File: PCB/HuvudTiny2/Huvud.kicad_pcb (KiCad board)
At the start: 4 copper layers, 42 x 42 mm, 98 parts, among them J1 Vin, J10 TC2, J12 USB_Micro-B, J2 DBG, J3 THERM, J4 FAN0, J5 FAN1, J6 Heater, J7 Endstop, J8 TC1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

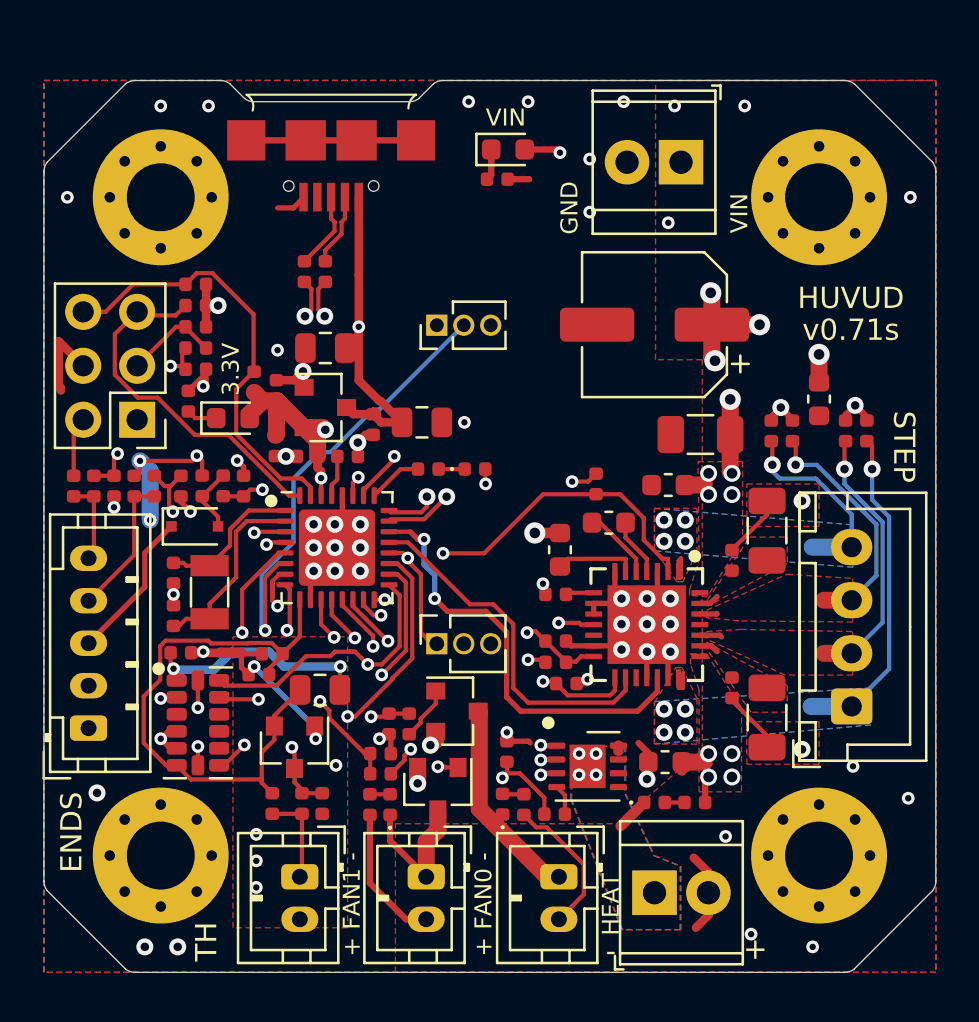
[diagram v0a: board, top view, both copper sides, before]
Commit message: Update PT board size and move filter cap on the Huvud so ethe two boards can actually be attached together.
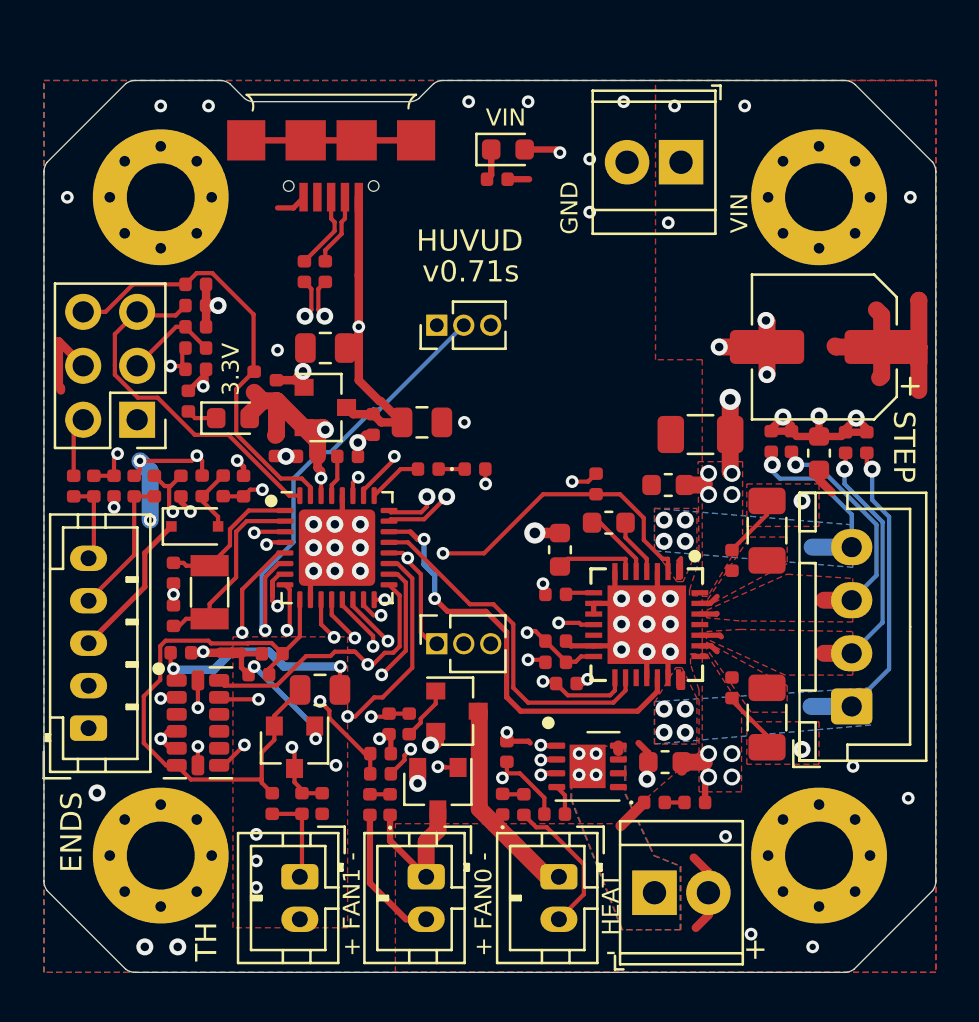
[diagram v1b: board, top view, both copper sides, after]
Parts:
- moved C8 8.07 mm to (218.8, 112.5)
- moved C16 2.55 mm to (218.5, 117.5), turned to 90 degrees
- moved C26 0.55 mm to (220.8, 117.0)
- moved C28 0.55 mm to (219.8, 117.0)
- moved C21 0.50 mm to (217.2, 117.0)
- moved C20 0.50 mm to (216.2, 117.0)
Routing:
- net GND: track 55.1 -> 65.6 mm, vias 57 -> 61
- net ST_VS: track 36.2 -> 43.0 mm, vias 24 -> 20
- net /ST_A2: track 17.0 -> 16.4 mm
- net /ST_A1: track 13.7 -> 13.2 mm
- net /ST_B2: track 11.0 -> 10.5 mm

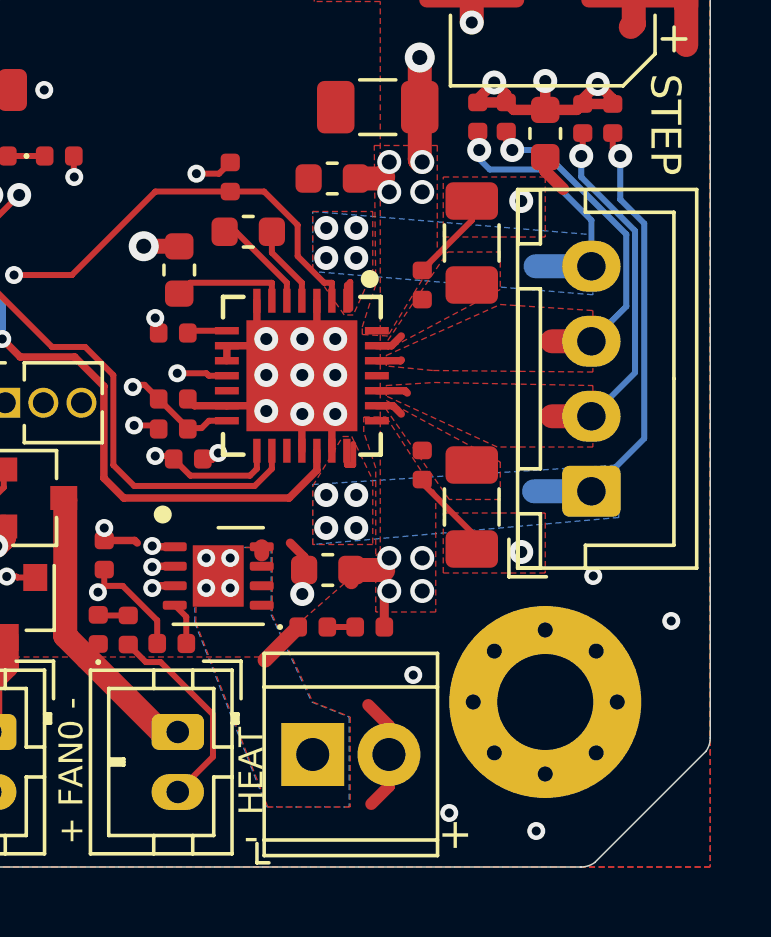
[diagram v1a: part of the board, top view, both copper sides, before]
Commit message: Improve sense resistor ground. Improve power mosfer routing. Set PCB color and copper finish.
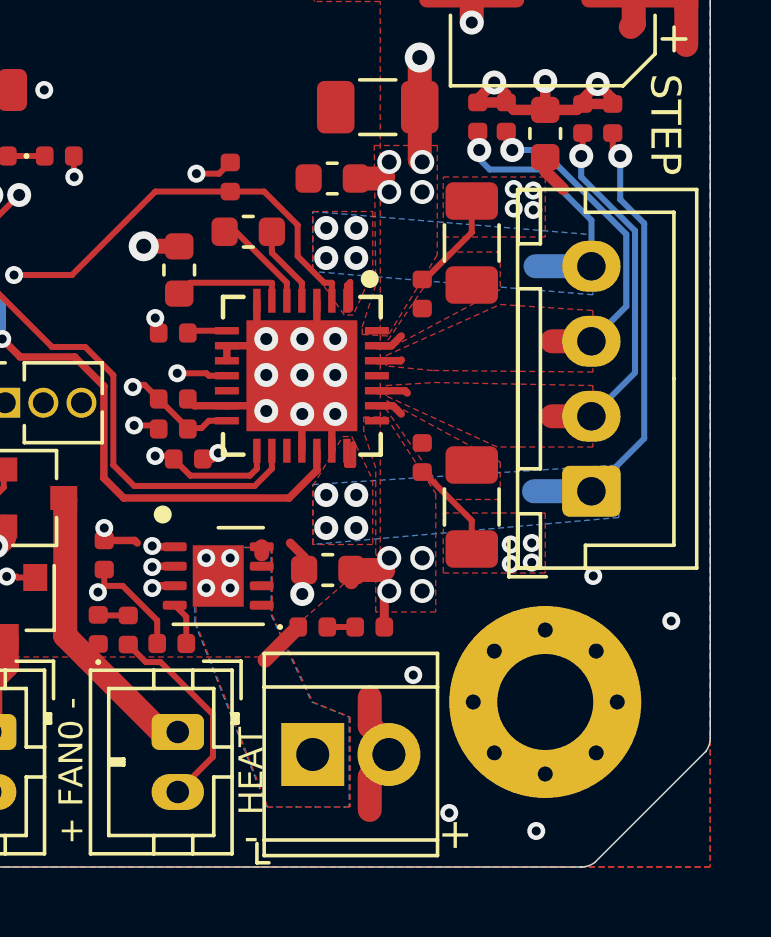
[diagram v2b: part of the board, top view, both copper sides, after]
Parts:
- moved C29 0.30 mm to (214.4, 122.9)
- moved C36 0.25 mm to (214.4, 128.3)
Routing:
- net ST_VS: track 43.0 -> 48.4 mm
- net GND: track 65.6 -> 66.2 mm, vias 61 -> 67
- added copper zone on In1.Cu, net Net-(D3-Pad1)

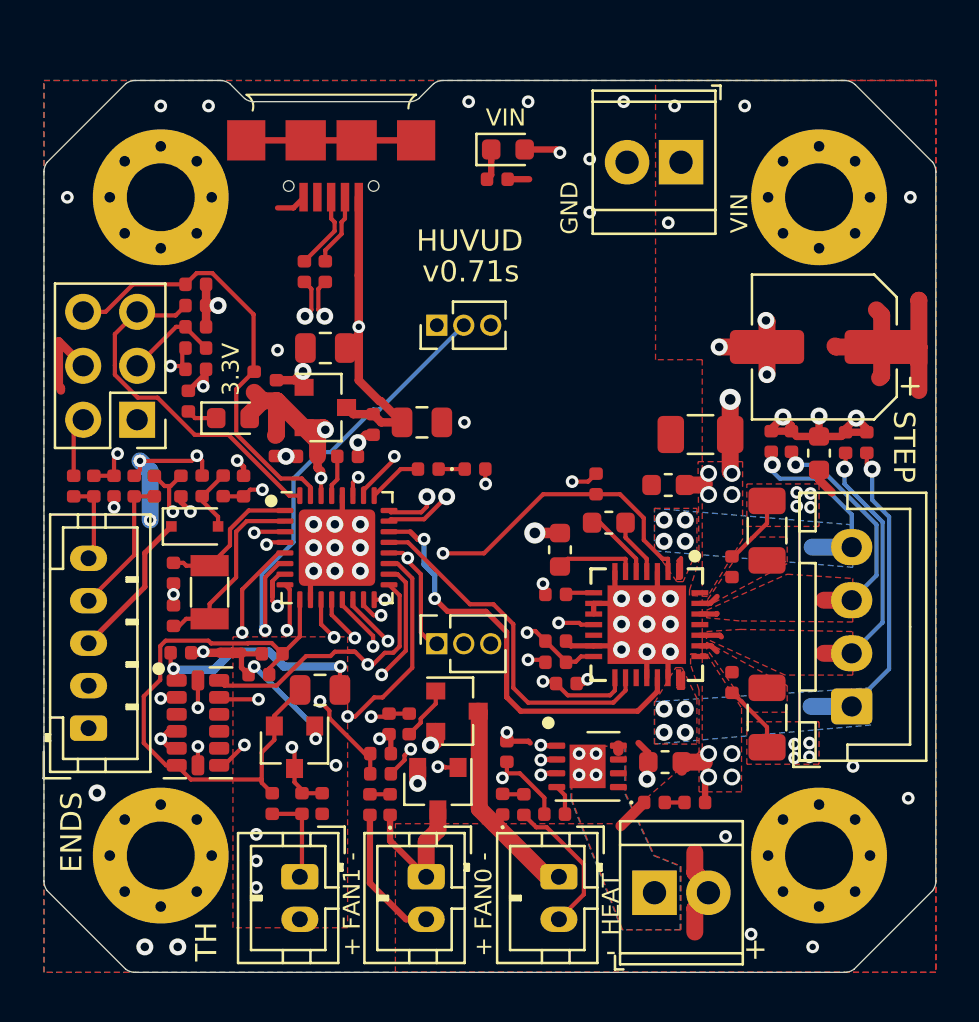
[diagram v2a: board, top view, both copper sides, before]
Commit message: Route new version with 1.25mm connectors. Added TH2 and 24V on the endstop connector.
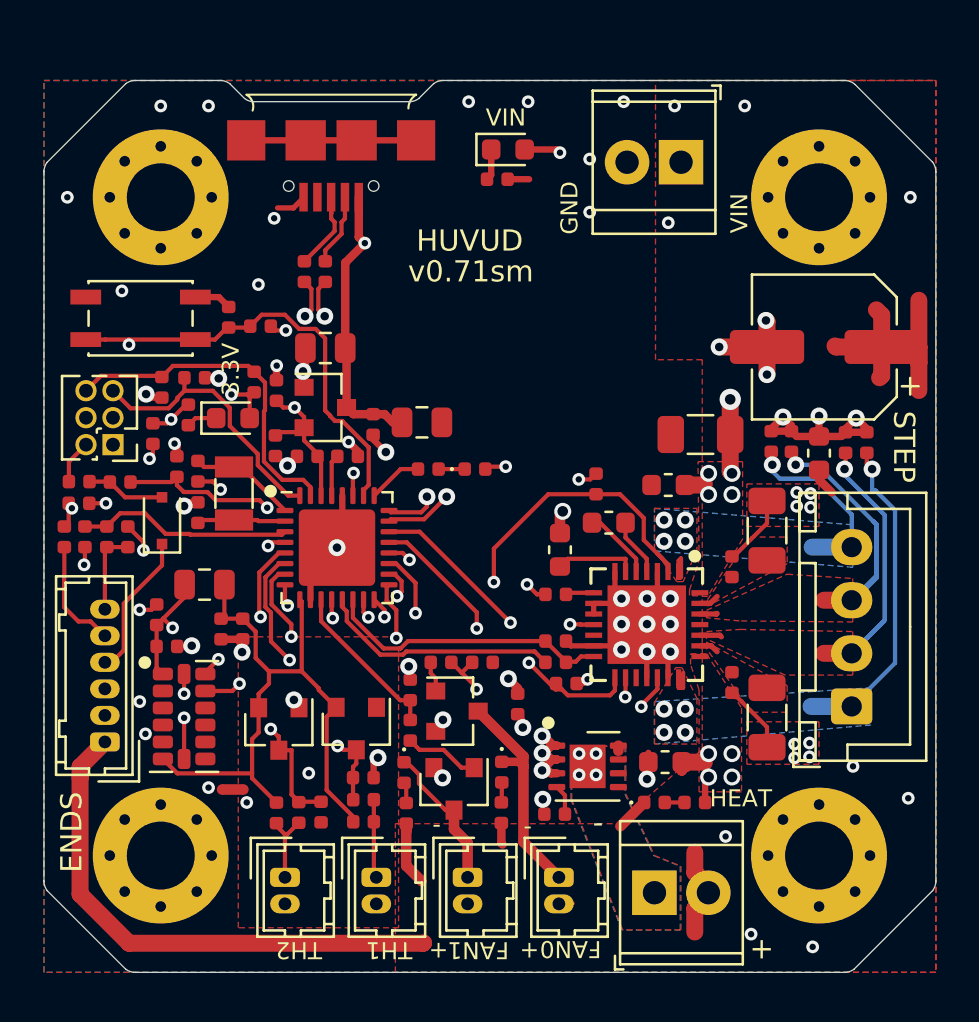
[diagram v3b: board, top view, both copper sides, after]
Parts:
- removed J10: TC2, Connector_PinHeader_1.27mm:PinHeader_1x03_P1.27mm_Vertical
- added C1: 0.1uF, Capacitor_SMD:C_0402_1005Metric, F.Cu at (195.1, 134.4)
- added D7: BAT54S, Package_TO_SOT_SMD:SOT-23, F.Cu at (193.1, 130.5)
- added R17: 10k, Resistor_SMD:R_0402_1005Metric, F.Cu at (194.0, 134.5)
- added R9: 4.7k, Resistor_SMD:R_0402_1005Metric, F.Cu at (192.9, 134.5)
- added SW1: SW_Push, Button_Switch_SMD:SW_SPST_EVQP2, F.Cu at (186.6, 111.2)
- J2: footprint Connector_PinHeader_2.54mm:PinHeader_2x03_P2.54mm_Vertical -> Connector_PinHeader_1.27mm:PinHeader_2x03_P1.27mm_Vertical
- J3, J4, J5: footprint Connector_JST:JST_PH_B2B-PH-K_1x02_P2.00mm_Vertical -> Connector_Hirose:Hirose_DF13-02P-1.25DSA_1x02_P1.25mm_Vertical
- J7: footprint Connector_JST:JST_PH_B5B-PH-K_1x05_P2.00mm_Vertical -> Connector_Hirose:Hirose_DF13-06P-1.25DSA_1x06_P1.25mm_Vertical
- J8: value TC1 -> THERM; footprint Connector_PinSocket_1.27mm:PinSocket_1x03_P1.27mm_Vertical -> Connector_Hirose:Hirose_DF13-02P-1.25DSA_1x02_P1.25mm_Vertical
- moved J8 13.1 mm to (193.3, 137.5), turned to -90 degrees
- moved L1 7.36 mm to (189.6, 123.7), turned to 0 degrees
- moved NT1 6.44 mm to (190.9, 133.4)
- moved R42 6.15 mm to (187.3, 125.2), turned to -90 degrees
- moved R32 5.79 mm to (183.7, 118.9), turned to 0 degrees
- moved R8 5.27 mm to (202.7, 127.4), turned to 180 degrees
- moved R21 5.11 mm to (187.6, 114.5), turned to 90 degrees
- moved C12 4.98 mm to (189.2, 120.3)
- moved C13 4.94 mm to (189.2, 118.4)
- moved C31 4.87 mm to (183.7, 119.9), turned to 0 degrees
- moved R43 4.87 mm to (183.0, 121.5)
- moved R33 4.85 mm to (185.6, 118.9), turned to 0 degrees
- moved Y1 4.79 mm to (190.9, 119.5)
- moved R2 4.39 mm to (197.1, 134.9), turned to 180 degrees
- moved C24 3.64 mm to (187.1, 116.6), turned to 90 degrees
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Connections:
- net THERM renamed THERM1
- J7 pad 1: GND -> ST_VS
- J7 pad 2: +5V -> GND
- J7 pad 3: Net-(D4-Pad1) -> +5V
- J7 pad 4: Net-(J7-Pad4) -> Net-(D4-Pad1)
- J8 pad 1: SDO -> Net-(J8-Pad1)
- J8 pad 2: SCL -> GNDA
- R19 pad 1: Net-(J7-Pad5) -> Net-(J7-Pad6)
- R36 pad 1: Net-(J7-Pad5) -> Net-(J7-Pad6)
- R42 pad 1: Net-(J7-Pad4) -> Net-(J7-Pad5)
- R43 pad 1: Net-(J7-Pad4) -> Net-(J7-Pad5)
- U1 pad 8: AINT1 -> (no net)
- U3 pad 5: AINT1 -> THERM2
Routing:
- net THERM1: track 31.9 -> 13.9 mm
- net +3V3: track 44.0 -> 29.1 mm, vias 10 -> 8
- net ST_VS: track 48.4 -> 63.1 mm
- net THERM2: track 0.00 -> 14.6 mm, vias 0 -> 2
- net AINT1: track 11.7 -> 0.00 mm, vias 2 -> 0
- net Net-(J7-Pad4): track 6.76 -> 0.00 mm
- net SCL: track 21.0 -> 14.4 mm
- net SDI: track 20.1 -> 14.6 mm, vias 1 -> 2
- net Net-(C12-Pad2): track 8.96 -> 4.18 mm
- net GNDA: track 7.87 -> 3.13 mm, vias 6 -> 5
- net ENDSTOP2: track 15.1 -> 19.8 mm
- net SWCLK: track 20.5 -> 16.1 mm
- net Net-(J7-Pad5): track 3.97 -> 8.36 mm, vias 0 -> 1
- net /ST_B1: track 11.8 -> 16.2 mm
- net FAN0: track 9.85 -> 14.0 mm
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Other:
- board text added: "FAN0"
- board text added: "FAN1"
- board text added: "IO RST nc"
- board text added: "TH1"
- board text added: "TH2"
- board text added: "Vin"
- board text added: "v0.71sm"
- board text removed: "+ FAN0 -"
- board text removed: "+ FAN1 -"
- board text removed: "3.3"
- board text removed: "CS"
- board text removed: "IO RST B1"
- board text removed: "SCL"
- board text removed: "SDI"
- board text removed: "SDO"
- board text removed: "TH"
- board text removed: "v0.71s"

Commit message: Switched power & USB to MOLEX MicroFit 2x6. Switched heater to 3.5mm terminal.
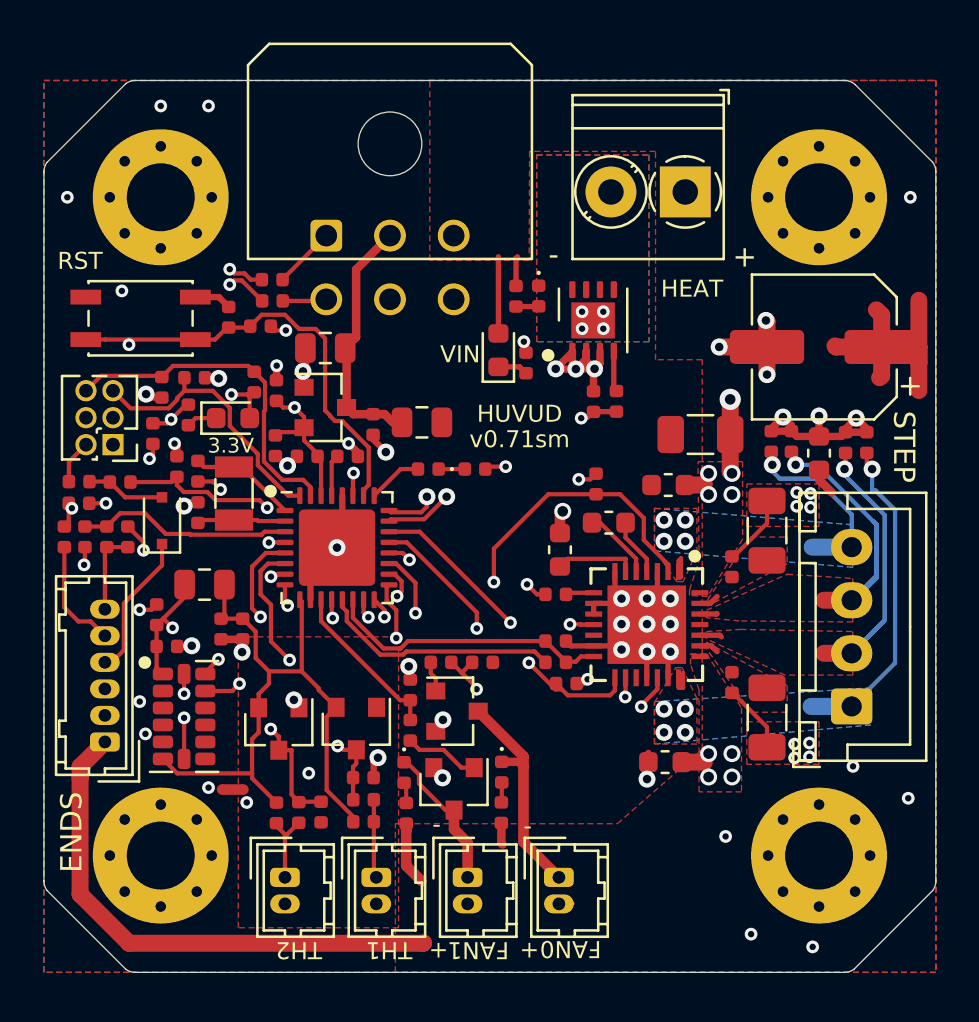
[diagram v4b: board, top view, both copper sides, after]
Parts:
- removed J12: USB_Micro-B, Huvud:MC-101C
- J1: value Vin -> MOLEX Micro Fit 2x3; footprint Huvud:TerminalBlock_TE_282834-2_1x02_P2.54mm_Horizontal -> Connector_Molex:Molex_Micro-Fit_3.0_43045-0600_2x03_P3.00mm_Horizontal
- J6: footprint Huvud:TerminalBlock_TE_282834-2_1x02_P2.54mm_Horizontal -> Huvud:TerminalBlock_Phoenix_PT-1,5-2-3.5-H_1x02_P3.50mm_Horizontal
- moved J6 33.0 mm to (212.2, 105.2), turned to 180 degrees
- moved R15 25.3 mm to (204.2, 110.2), turned to -90 degrees
- moved D3 24.5 mm to (205.3, 110.2), turned to -90 degrees
- moved Q3 21.0 mm to (207.9, 111.3), turned to 90 degrees
- moved R28 19.7 mm to (209.0, 115.1), turned to 90 degrees
- moved LOGO1 17.2 mm to (205.7, 132.2)
- moved J1 17.1 mm to (195.3, 107.3), turned to 0 degrees
- moved R12 14.7 mm to (207.9, 115.1)
- moved D6 9.46 mm to (203.4, 112.7), turned to 90 degrees
- moved R11 8.75 mm to (204.7, 113.3), turned to 90 degrees
- moved R26 2.53 mm to (192.8, 109.4), turned to 0 degrees
- moved R25 2.04 mm to (192.8, 110.4), turned to 0 degrees
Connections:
- J1 pad 1: ST_VS -> /D-
- J1 pad 2: GND -> +5V
- J6 pad 1: Net-(D3-Pad1) -> ST_VS
- J6 pad 2: ST_VS -> Net-(D3-Pad1)
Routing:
- net unconnected-(J12-Pad6): track 8.00 -> 0.00 mm
- net HEATER: track 22.7 -> 30.4 mm, vias 3 -> 2
- net USBD-: track 16.5 -> 21.5 mm
- net USBD+: track 16.0 -> 20.4 mm
- net ST_VS: track 63.1 -> 60.3 mm, vias 20 -> 16
- net GND: track 63.8 -> 66.0 mm, vias 62 -> 55
- net /D+: track 3.93 -> 2.08 mm
- net Net-(D3-Pad1): track 1.82 -> 0.00 mm
- net +5V: track 13.3 -> 11.9 mm, vias 1 -> 0
- net ST_EN: track 23.3 -> 22.3 mm
- net /D-: track 3.66 -> 2.93 mm
- net THERM2: track 14.6 -> 15.2 mm
- net Net-(D6-Pad1): track 2.00 -> 1.42 mm
- removed copper zone on In1.Cu, net Net-(D3-Pad1)
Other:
- outline, holes or cut-outs redrawn
- board text added: "D+"
- board text added: "D-"
- board text added: "RST"
- board text removed: "GND"
